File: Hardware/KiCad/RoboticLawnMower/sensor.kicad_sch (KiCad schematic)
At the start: 4 parts, among them J19 Conn_01x03, J20 Conn_01x03, J21 Conn_01x03, J22 Conn_01x03

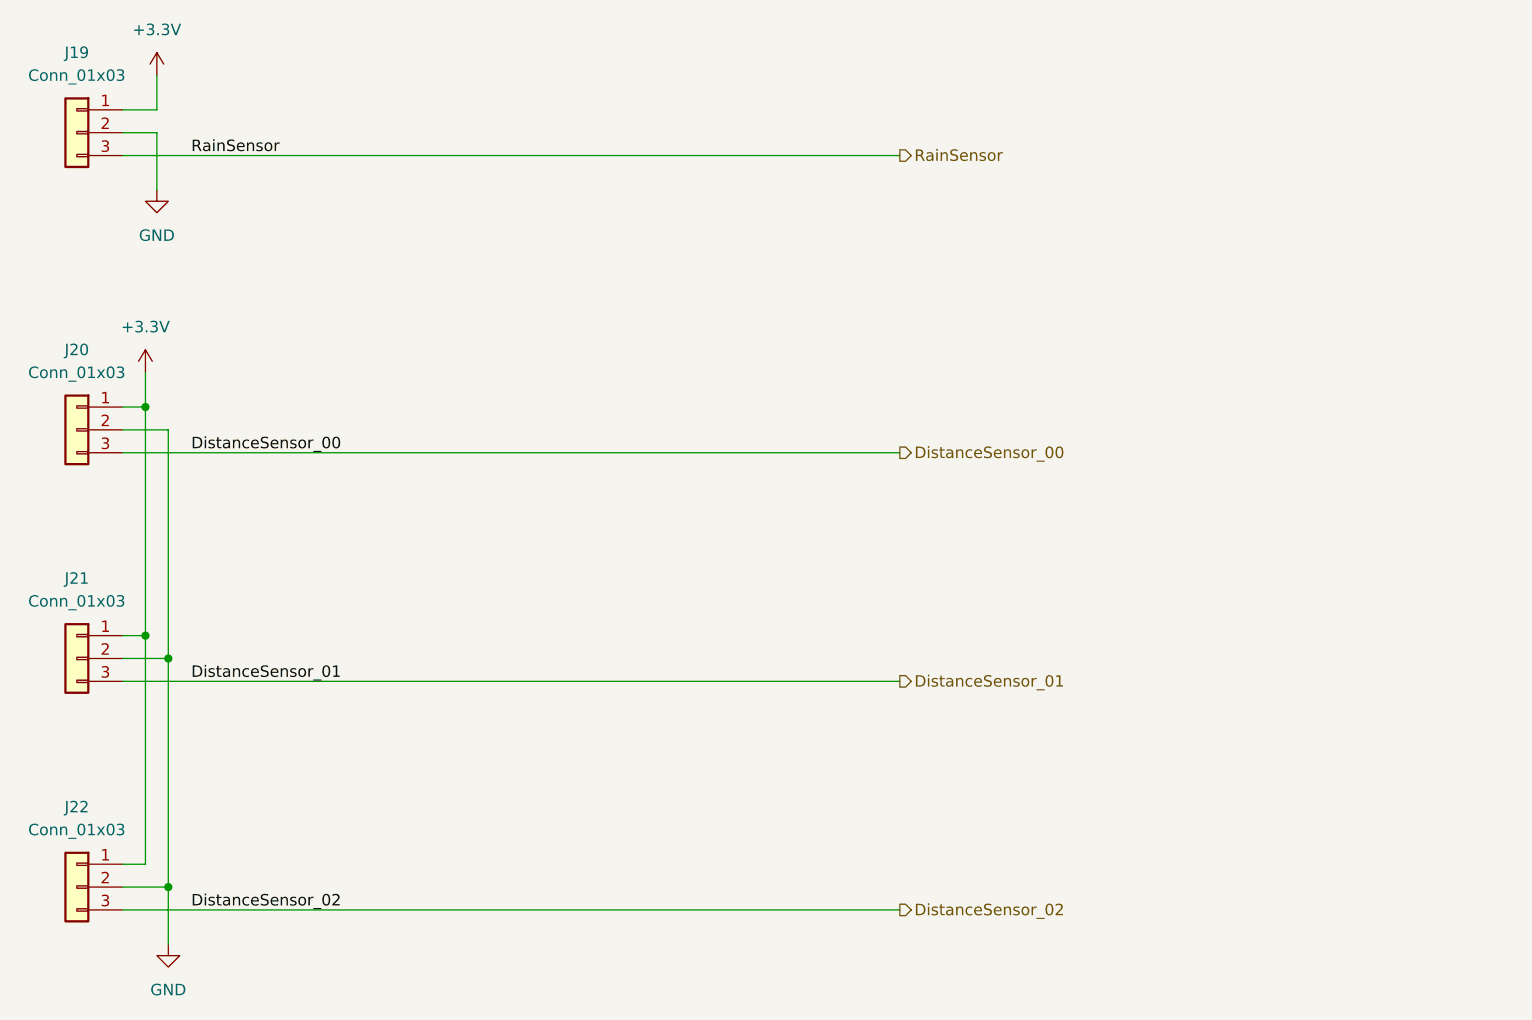
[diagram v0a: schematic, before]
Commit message: Schaltplan & Layout Änderung
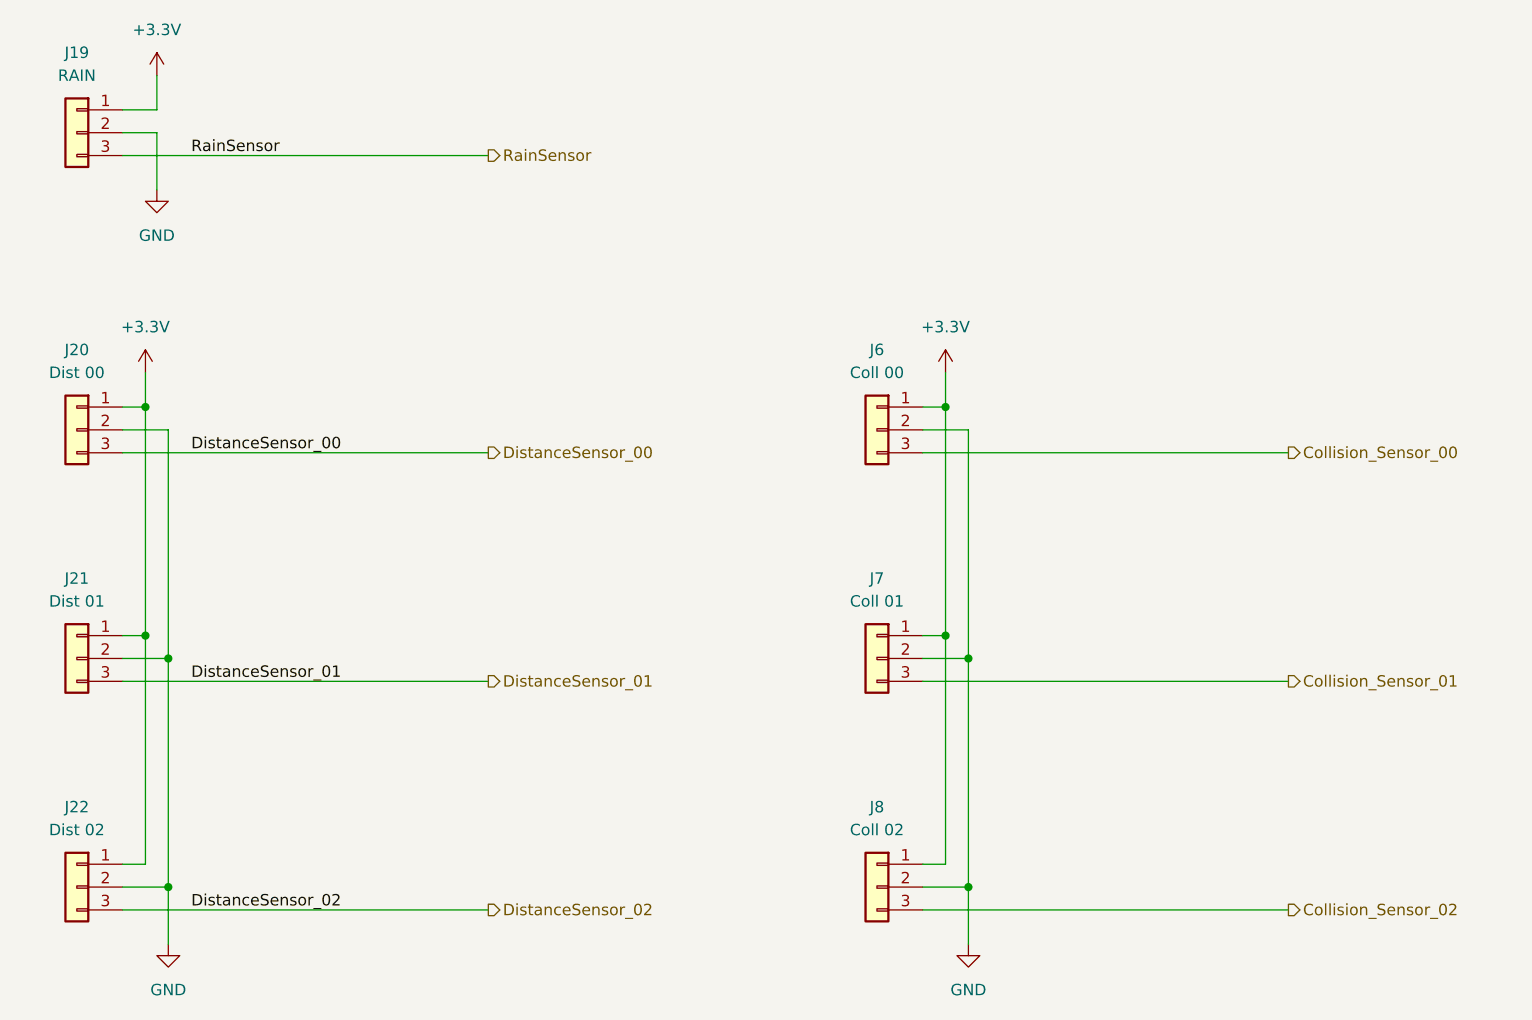
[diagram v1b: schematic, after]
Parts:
- added J6: Coll 00, Connector_JST:JST_XA_B03B-XASK-1_1x03_P2.50mm_Vertical, symbol Connector_Generic:Conn_01x03
- added J7: Coll 01, Connector_JST:JST_XA_B03B-XASK-1_1x03_P2.50mm_Vertical, symbol Connector_Generic:Conn_01x03
- added J8: Coll 02, Connector_JST:JST_XA_B03B-XASK-1_1x03_P2.50mm_Vertical, symbol Connector_Generic:Conn_01x03
- J19: value Conn_01x03 -> RAIN
- J20: value Conn_01x03 -> Dist 00
- J21: value Conn_01x03 -> Dist 01
- J22: value Conn_01x03 -> Dist 02
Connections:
- net +3.3V: now also J6.1 (Pin_1), J7.1 (Pin_1), J8.1 (Pin_1)
- net GND: now also J6.2 (Pin_2), J7.2 (Pin_2), J8.2 (Pin_2)
- new net Collision_Sensor_00: J6.3 (Pin_3)
- new net Collision_Sensor_01: J7.3 (Pin_3)
- new net Collision_Sensor_02: J8.3 (Pin_3)
